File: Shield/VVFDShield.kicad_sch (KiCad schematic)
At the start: 18 parts, among them J1 Conn_02x05_Counter_Clockwise, J2 Conn_02x05_Counter_Clockwise, P1 Power, P2 Digital, P3 Digital, P4 Analog, SW1 SW_SPST, SW2 SW_SPST

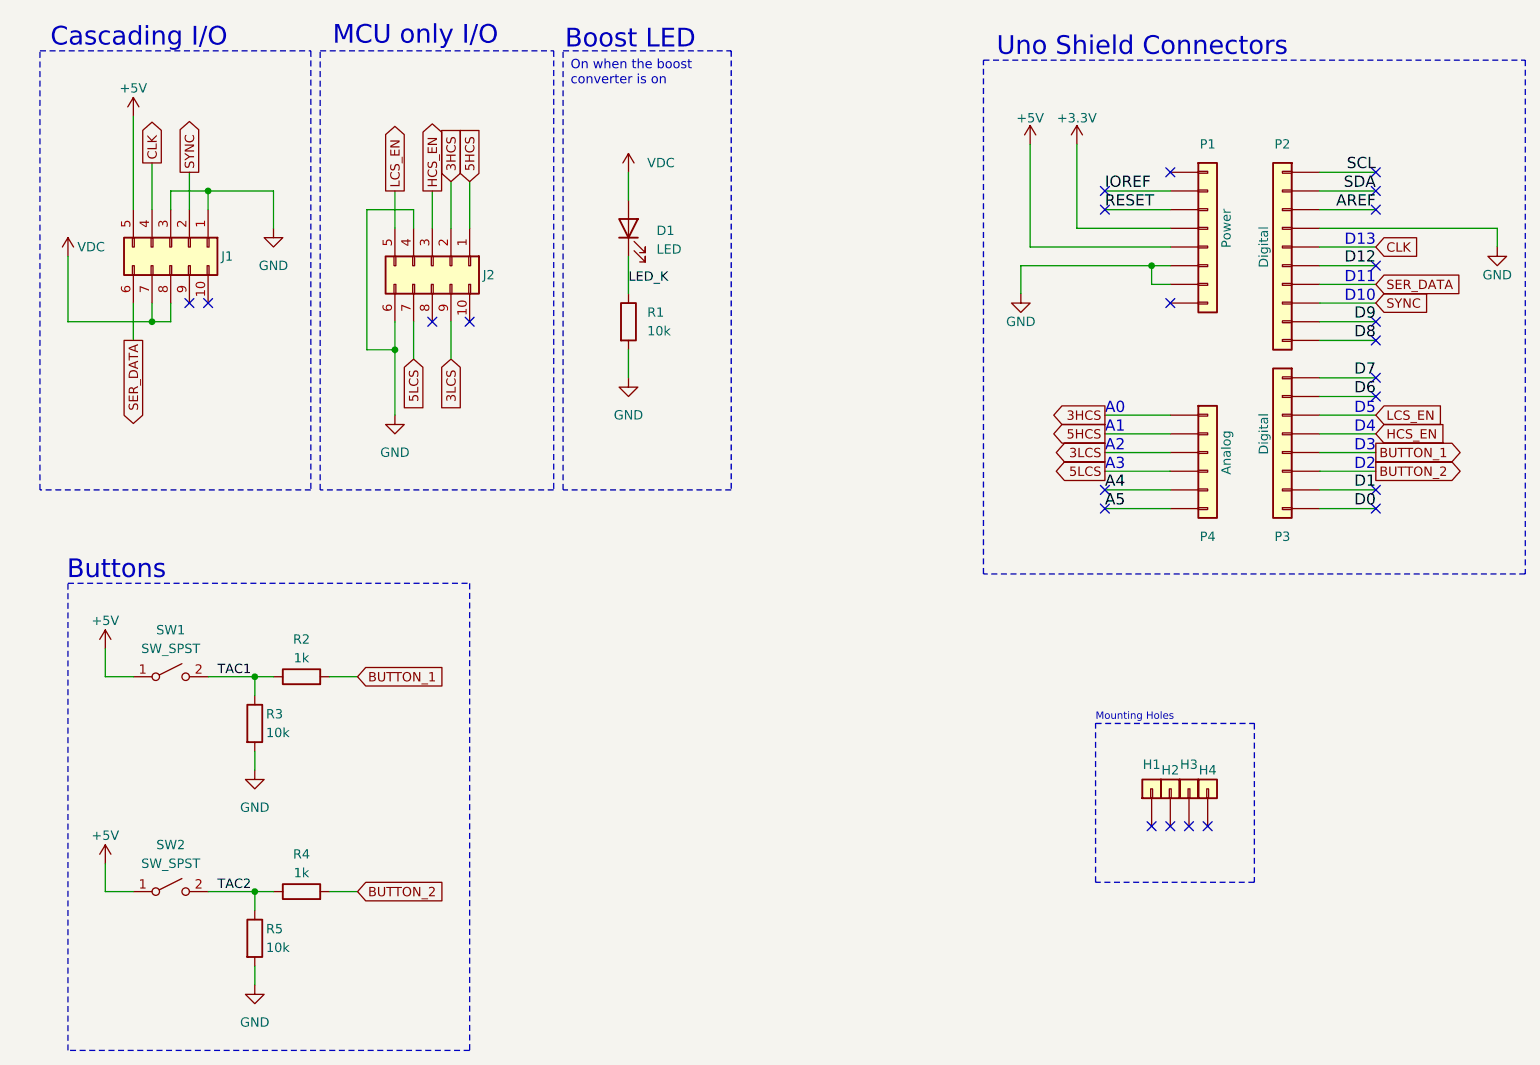
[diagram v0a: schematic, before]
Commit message: Removed Current Sensing
Removed current sensing, because it would require a major design
overhaul to work properly.
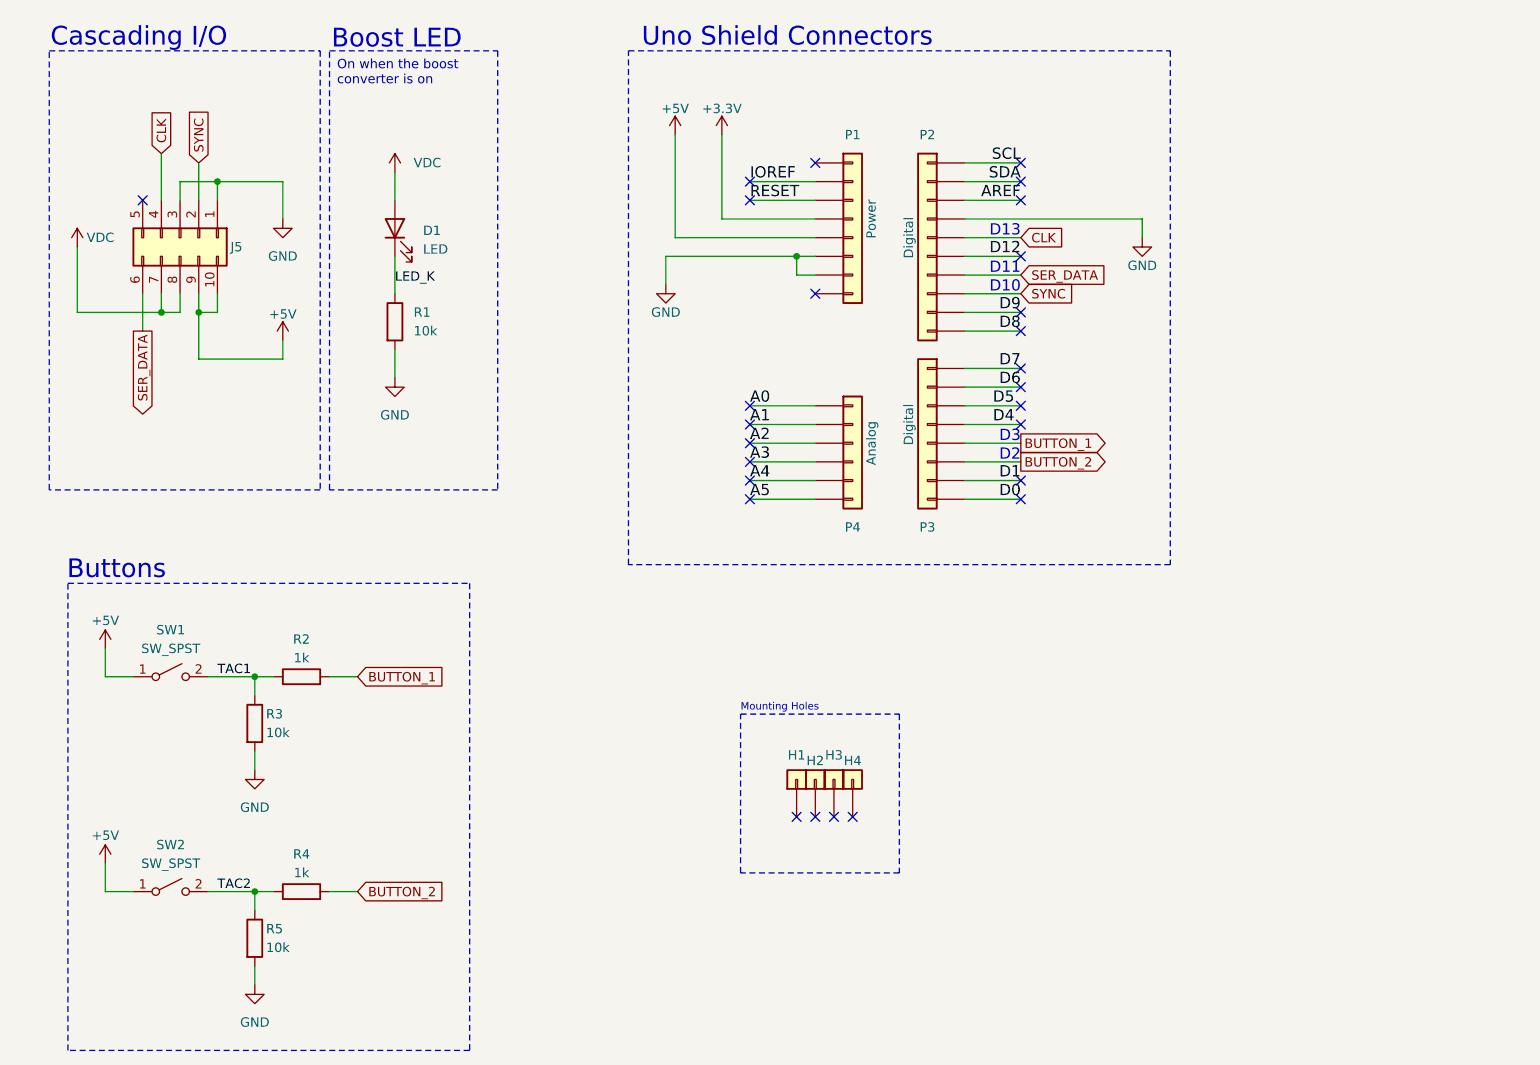
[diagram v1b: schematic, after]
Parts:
- removed J2: Conn_02x05_Counter_Clockwise, Connector_IDC:IDC-Header_2x05_P2.54mm_Vertical, symbol Connector_Generic:Conn_02x05_Counter_Clockwise
- renumbered J1 to J5
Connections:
- net +5V: now also J5.10 (Pin_10), J5.9 (Pin_9); no longer J5.5 (Pin_5)
- net 3HCS renamed A0
- net 3LCS renamed A2
- net 5HCS renamed A1
- net 5LCS renamed A3
- net HCS_EN renamed D4
- net LCS_EN renamed D5
- no-connect marks 24 -> 27
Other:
- note removed: "A0"
- note removed: "A1"
- note removed: "A2"
- note removed: "A3"
- note removed: "D4"
- note removed: "D5"
- note removed: "MCU only I/O"
- moved on the sheet: D1, H1, H2, H3, H4, J5, P1, P2, P3, P4, R1
